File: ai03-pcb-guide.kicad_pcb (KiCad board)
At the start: 2 copper layers, 24 parts, among them SW1 SW_Push, U1 ATmega32U4-AU, Y1 16MHz

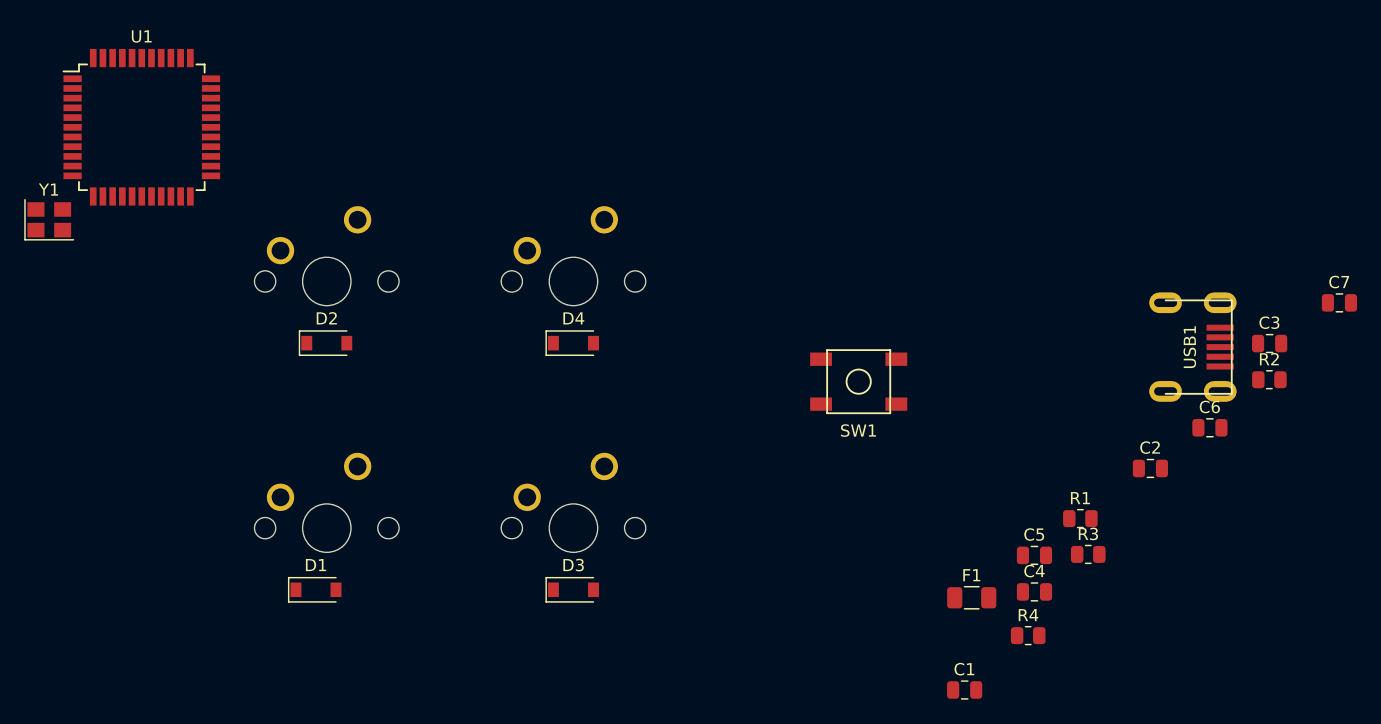
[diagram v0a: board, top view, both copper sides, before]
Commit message: added ground fill, black soldermask, micro usb error still persists
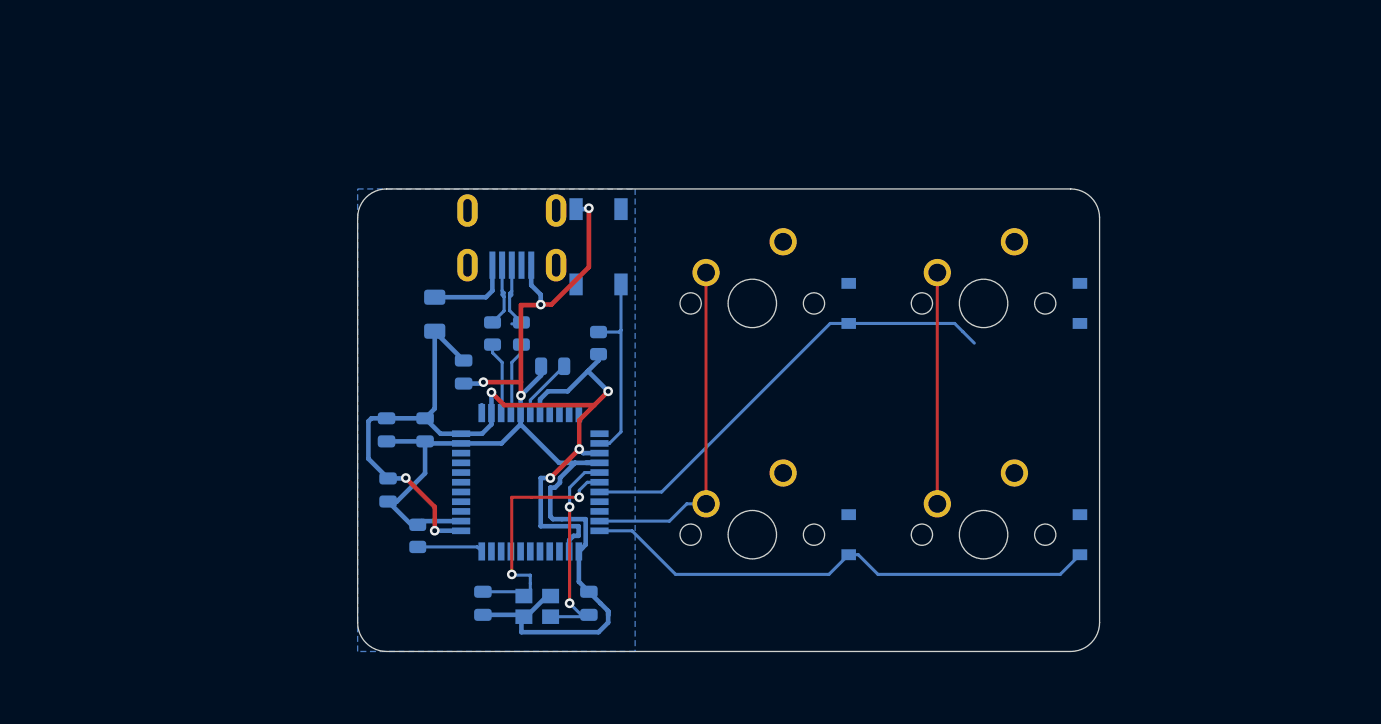
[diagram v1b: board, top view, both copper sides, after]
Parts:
- C1, C2, C3, C4, C5, C6, C7, D1, D2, D3, D4, F1, R1, R2, R3, R4, SW1, U1, USB1, Y1: moved to B.Cu
- moved C7 65.0 mm to (54.2, 40.0), turned to 180 degrees
- moved C6 64.7 mm to (43.7, 45.2), turned to 270 degrees
- moved R2 61.7 mm to (51.6, 37.3), turned to 90 degrees
- moved C3 60.0 mm to (57.1, 59.5), turned to 90 degrees
- moved C2 56.1 mm to (48.4, 59.5), turned to 270 degrees
- moved USB1 55.0 mm to (50.8, 27.2), turned to 270 degrees
- moved C5 54.4 mm to (40.5, 45.2), turned to 270 degrees
- moved Y1 51.3 mm to (52.9, 59.8)
- moved R4 51.0 mm to (43.1, 54.0), turned to 270 degrees
- moved R1 50.8 mm to (49.2, 37.3), turned to 90 degrees
- moved C4 50.4 mm to (46.8, 40.5), turned to 270 degrees
- moved C1 50.3 mm to (40.6, 50.2), turned to 270 degrees
- moved F1 50.0 mm to (44.5, 35.7), turned to 90 degrees
- moved D3 47.9 mm to (97.6, 34.8), turned to 90 degrees
- moved D4 44.6 mm to (97.6, 53.9), turned to 90 degrees
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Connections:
- U1 pad 18: Net-(U1-Pad18) -> ROW0
- U1 pad 20: Net-(U1-Pad20) -> COL1
- U1 pad 21: Net-(U1-Pad21) -> COL0
- U1 pad 22: Net-(U1-Pad22) -> ROW1
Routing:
- net GND: track 0.00 -> 103.8 mm, vias 0 -> 4
- net +5V: track 0.00 -> 79.5 mm, vias 0 -> 6
- net ROW1: track 0.00 -> 43.1 mm
- net ROW0: track 0.00 -> 37.3 mm
- net COL0: track 0.00 -> 28.4 mm
- net Net-(C2-Pad1): track 0.00 -> 21.4 mm, vias 0 -> 2
- net COL1: track 0.00 -> 19.1 mm
- net Net-(C3-Pad1): track 0.00 -> 17.7 mm, vias 0 -> 2
- net Net-(R3-Pad2): track 0.00 -> 16.2 mm
- net VCC: track 0.00 -> 6.66 mm
- net Net-(R2-Pad1): track 0.00 -> 6.12 mm
- net Net-(R1-Pad1): track 0.00 -> 6.01 mm
- net D+: track 0.00 -> 5.97 mm
- net Net-(R4-Pad2): track 0.00 -> 5.79 mm
- net D-: track 0.00 -> 5.67 mm
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- added copper zone on B.Cu, net GND
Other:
- board outline added: 61.1 x 38.1 mm
- net class Default: trace_width 0.25 -> 0.254
- net class Power added: clearance 0.2, trace_width 0.381, via_dia 0.8, via_drill 0.4

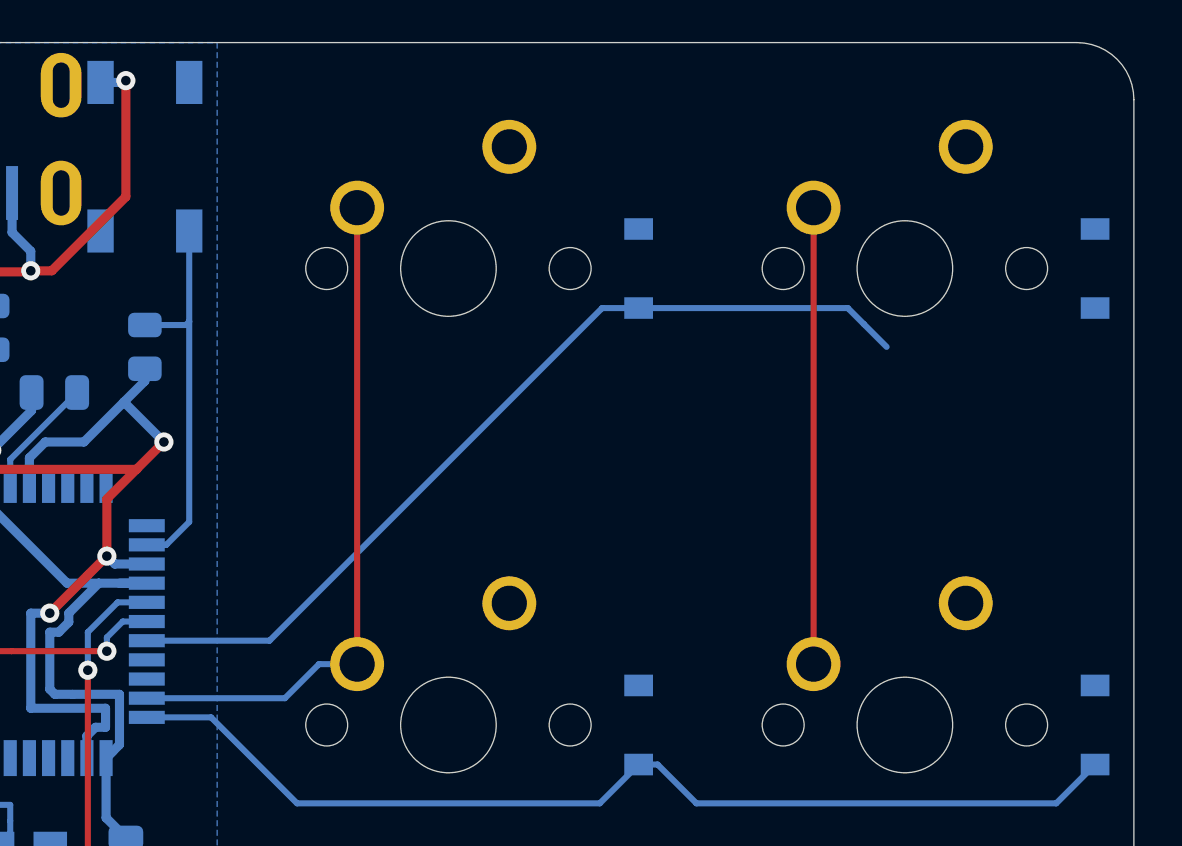
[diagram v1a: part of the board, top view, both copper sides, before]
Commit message: added missing traces
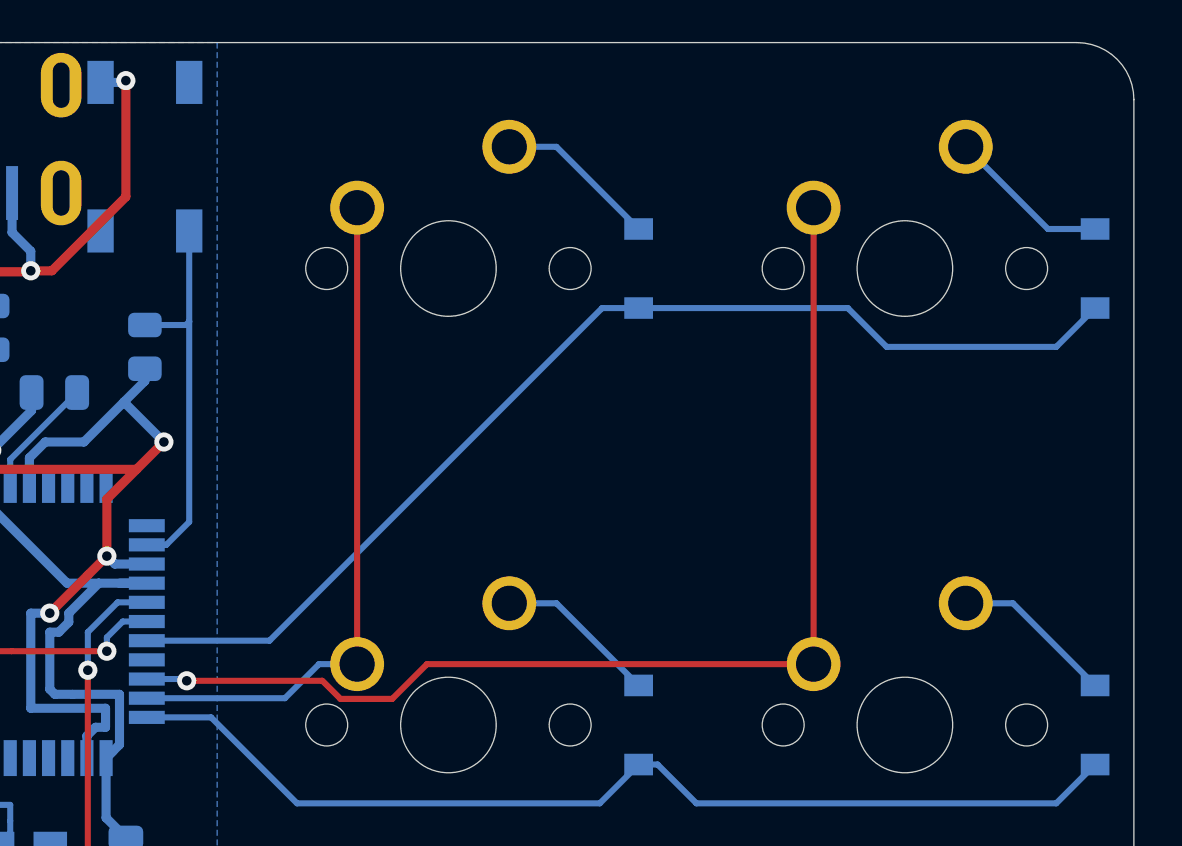
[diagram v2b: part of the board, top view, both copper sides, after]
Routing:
- net COL1: track 19.1 -> 47.8 mm, vias 0 -> 1
- net ROW0: track 37.3 -> 46.7 mm
- net Net-(D4-Pad2): track 0.00 -> 6.82 mm
- net Net-(D3-Pad2): track 0.00 -> 6.82 mm
- net Net-(D2-Pad2): track 0.00 -> 6.82 mm
- net Net-(D1-Pad2): track 0.00 -> 6.82 mm

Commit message: more trace fixes
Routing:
- net Net-(USB1-Pad6): track 0.21 -> 16.5 mm
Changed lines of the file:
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@@
     (thickness 1.6)
     (drawings 8)
-    (tracks 232)
+    (tracks 235)
     (zones 0)
     (modules 24)
@@
   (segment (start 48.324 43.21475) (end 48.324 43.86175) (width 0.381) (layer B.Cu) (net 42))
   (segment (start 47.15 32.28125) (end 47.15 32.06875) (width 0.254) (layer B.Cu) (net 43))
+  (segment (start 47.15 31.678) (end 47.15 27.178) (width 0.254) (layer B.Cu) (net 43))
+  (segment (start 47.15 27.178) (end 54.45 27.178) (width 0.254) (layer B.Cu) (net 43))
+  (segment (start 54.45 27.178) (end 54.45 31.678) (width 0.254) (layer B.Cu) (net 43))
   (zone (net 1) (net_name GND) (layer B.Cu) (hatch edge 0.508)
     (connect_pads (clearance 0.508))
     (min_thickness 0.254)
-    (fill yes (arc_segments 32) (thermal_gap 0.508) (thermal_bridge_width 0.508))
+    (fill (arc_segments 32) (thermal_gap 0.508) (thermal_bridge_width 0.508))
     (polygon
       (pts

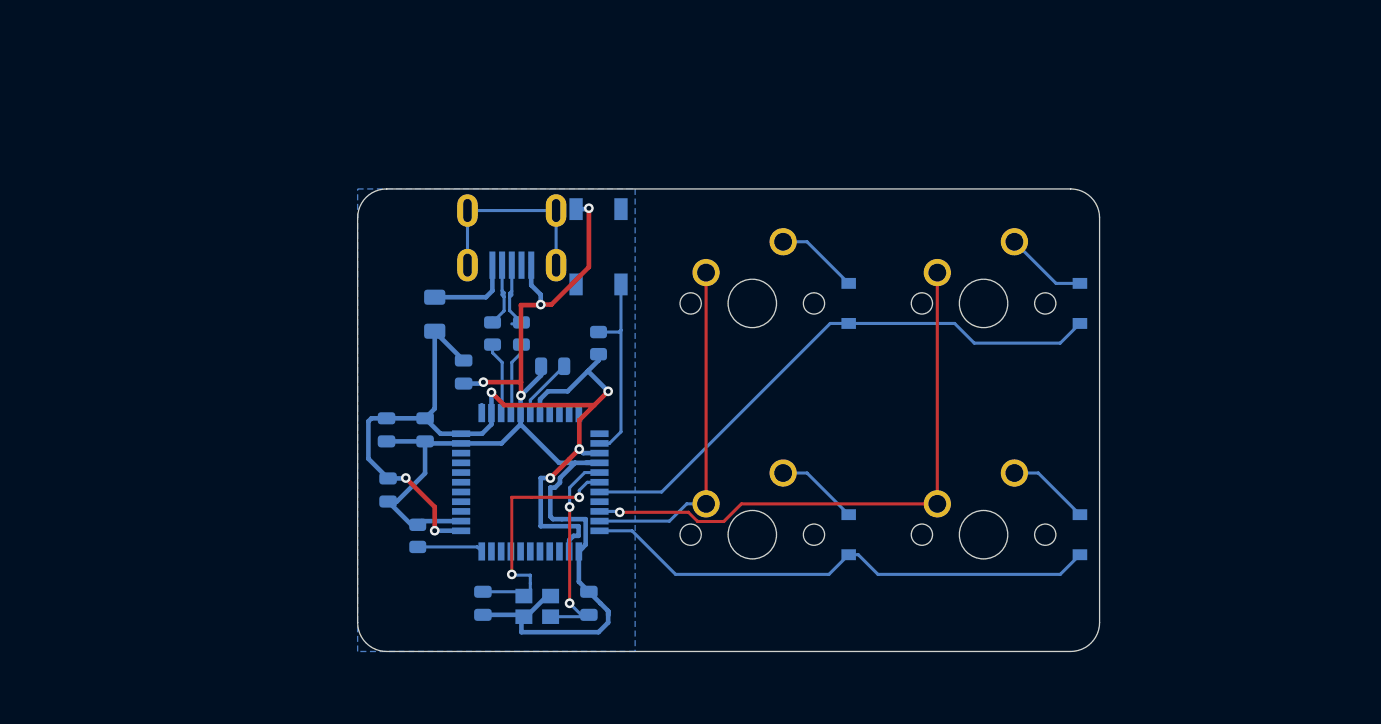
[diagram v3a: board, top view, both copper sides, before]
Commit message: redid pcb layout and routing
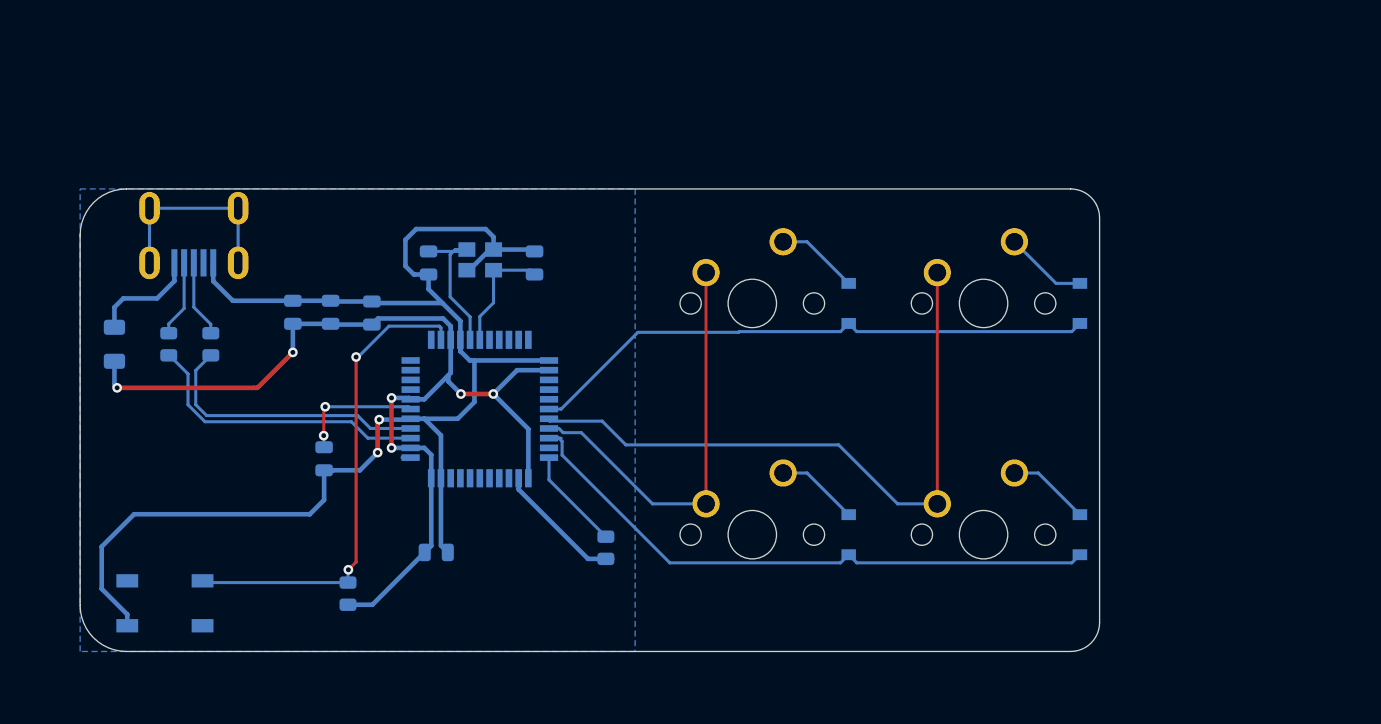
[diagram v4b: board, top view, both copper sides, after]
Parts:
- moved SW1 46.2 mm to (22.2, 59.5), turned to 180 degrees
- moved C3 31.0 mm to (43.9, 31.5), turned to 270 degrees
- moved R3 29.2 mm to (37.3, 58.7)
- moved Y1 28.9 mm to (48.2, 31.2), turned to 180 degrees
- moved C2 28.4 mm to (52.7, 31.5), turned to 90 degrees
- moved R1 26.7 mm to (22.5, 38.2)
- moved F1 26.5 mm to (18.1, 38.2)
- moved USB1 26.2 mm to (24.6, 27.0)
- moved R2 25.6 mm to (26.0, 38.2)
- moved C7 20.3 mm to (35.3, 47.6), turned to 270 degrees
- moved R4 15.5 mm to (58.5, 55.0), turned to 90 degrees
- moved C1 14.6 mm to (39.3, 35.6), turned to 90 degrees
- moved C5 12.4 mm to (32.8, 35.6), turned to 90 degrees
- moved C4 12.0 mm to (35.9, 35.6), turned to 90 degrees
- moved C6 10.1 mm to (44.6, 55.3), turned to 0 degrees
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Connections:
- U1 pad 18: ROW0 -> Net-(U1-Pad18)
- U1 pad 20: COL1 -> Net-(U1-Pad20)
- U1 pad 21: COL0 -> Net-(U1-Pad21)
- U1 pad 22: ROW1 -> Net-(U1-Pad22)
- U1 pad 28: Net-(U1-Pad28) -> ROW0
- U1 pad 29: Net-(U1-Pad29) -> COL1
- U1 pad 30: Net-(U1-Pad30) -> COL0
- U1 pad 31: Net-(U1-Pad31) -> ROW1
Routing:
- net GND: track 103.8 -> 131.1 mm, vias 4 -> 2
- net Net-(R3-Pad2): track 16.2 -> 40.0 mm, vias 0 -> 2
- net Net-(R1-Pad1): track 6.01 -> 24.4 mm
- net Net-(R2-Pad1): track 6.12 -> 23.3 mm
- net Net-(C2-Pad1): track 21.4 -> 10.2 mm, vias 2 -> 0
- net ROW1: track 43.1 -> 50.8 mm
- net COL1: track 47.8 -> 54.0 mm, vias 1 -> 0
- net +5V: track 79.5 -> 85.7 mm
- net COL0: track 28.4 -> 34.6 mm
- net Net-(C7-Pad1): track 5.14 -> 10.6 mm, vias 0 -> 2
- net Net-(C3-Pad1): track 17.7 -> 12.7 mm, vias 2 -> 0
- net Net-(R4-Pad2): track 5.79 -> 8.83 mm
- net VCC: track 6.66 -> 9.17 mm
- net D-: track 5.67 -> 6.84 mm
- net ROW0: track 46.7 -> 47.5 mm
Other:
- board size 61.1 x 38.1 mm -> 84 x 38.1 mm
